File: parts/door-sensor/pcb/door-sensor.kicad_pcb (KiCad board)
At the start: 2 copper layers, 48.3 x 36.8 mm, 10 parts, among them J2 RJ45_Shielded, J3 Screw_Terminal_01x03

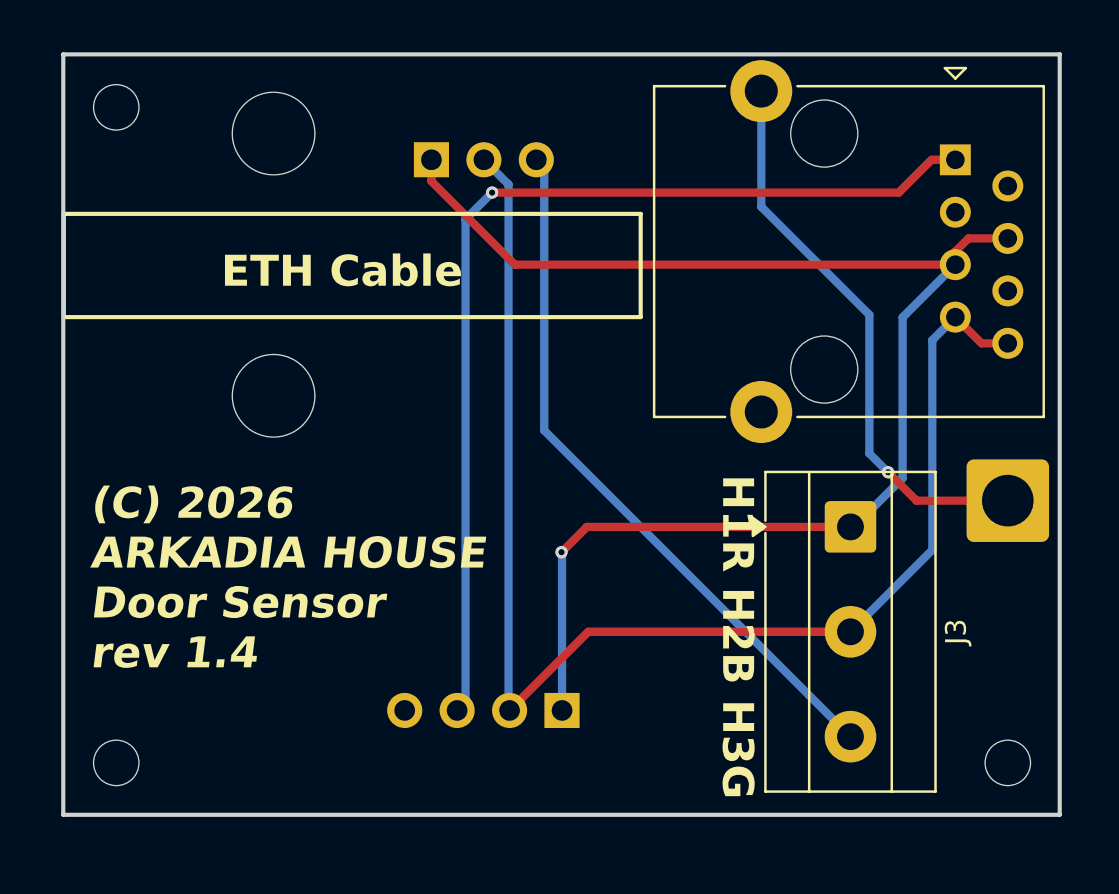
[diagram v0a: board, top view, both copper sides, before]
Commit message: pcb revisions to update to better RJ45 jack, update QR code.
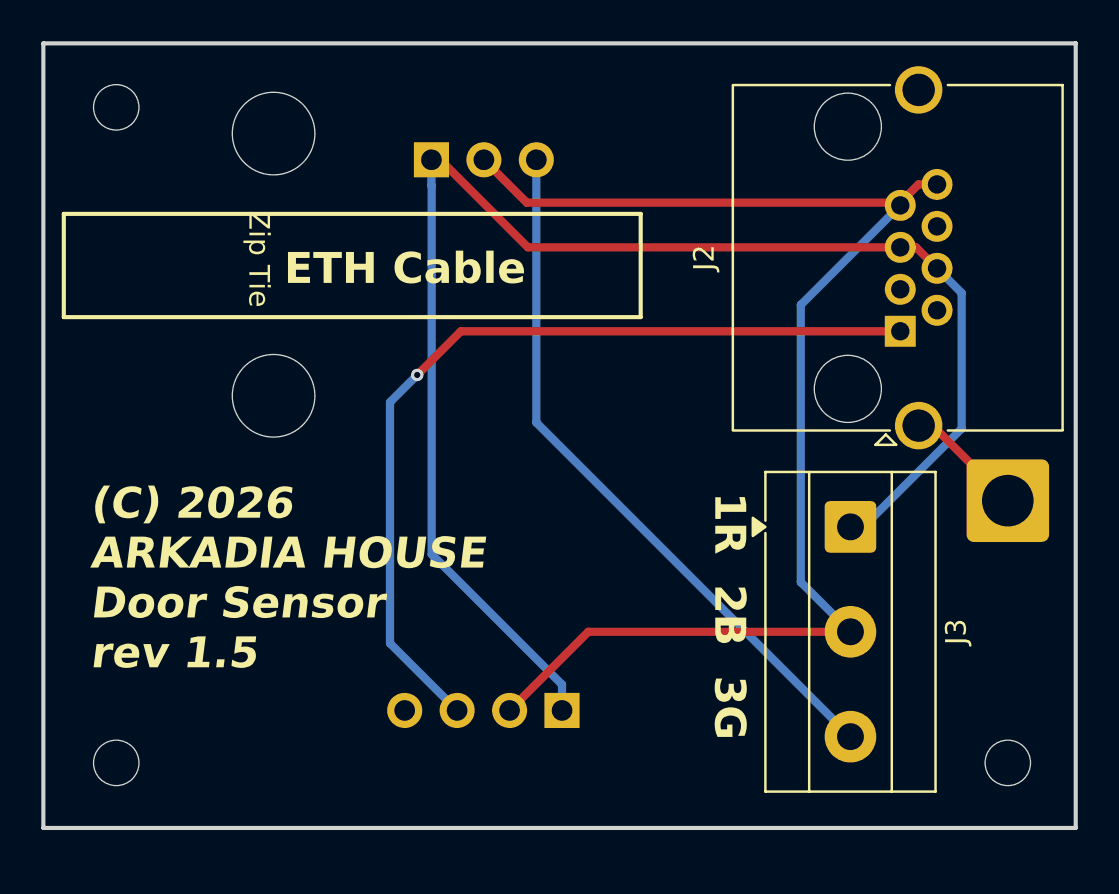
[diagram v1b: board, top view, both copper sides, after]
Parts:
- J2: footprint Connector_RJ:RJ45_Ninigi_GE -> Connector_RJ:RJ45_Amphenol_RJHSE5380
- moved J2 8.72 mm to (174.7, 59.1), turned to 90 degrees
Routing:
- net unconnected-(J2-PadSH): track 27.4 -> 5.14 mm, vias 1 -> 0
- net /SENSE: track 48.9 -> 42.4 mm
- net /5V: track 68.9 -> 70.5 mm, vias 1 -> 0
- net /GND: track 65.7 -> 64.9 mm
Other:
- board size 48.3 x 36.8 mm -> 50 x 38 mm
- board text added: "(C) 2026 ARKADIA HOUSE Door Sensor rev 1.5"
- board text added: "1R 2B 3G"
- board text added: "Zip Tie"
- board text removed: "(C) 2026 ARKADIA HOUSE Door Sensor rev 1.4"
- board text removed: "H1R H2B H3G"
